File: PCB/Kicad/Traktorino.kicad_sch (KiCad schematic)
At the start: 5 parts, among them J1 analog_pins, J2 mux_pins, J3 595_pins, J4 d13

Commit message: update elements WIP
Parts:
- removed J1: analog_pins, Pin_Headers:Pin_Header_Straight_1x07_Pitch2.54mm, symbol Traktorino-rescue:CONN_01X07
- removed J2: mux_pins, Pin_Headers:Pin_Header_Straight_1x06_Pitch2.54mm, symbol Traktorino-rescue:CONN_01X06
- removed J3: 595_pins, Pin_Headers:Pin_Header_Straight_1x05_Pitch2.54mm, symbol Traktorino-rescue:CONN_01X05
- removed J4: d13, Pin_Headers:Pin_Header_Straight_1x03_Pitch2.54mm, symbol Traktorino-rescue:CONN_01X03
- removed SHIELD1: ARDUINO_SHIELD, arduino_shields:ARDUINO_SHIELD_2_040pins, symbol Traktorino-rescue:ARDUINO_SHIELD
- added A1: Arduino_UNO_R3, Module:Arduino_UNO_R2, symbol MCU_Module:Arduino_UNO_R2
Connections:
- net A0: now also A1.9 (A0)
- net A1: now also A1.10 (A1)
- net A2: now also A1.11 (A2)
- net A3: now also A1.12 (A3)
- net A4: now also A1.13 (SDA/A4)
- net A5: now also A1.14 (SCL/A5)
- net D11: now also A1.26 (D11)
- net D12: now also A1.27 (D12)
- net D13: now also A1.28 (D13)
- net D2: now also A1.17 (D2)
- net D3: now also A1.18 (D3)
- net D4: now also A1.19 (D4)
- net D5: now also A1.20 (D5)
- net D6: now also A1.21 (D6)
- net D7: now also A1.22 (D7)
- net D8: now also A1.23 (D8)
- net GND: now also A1.29 (GND), A1.6 (GND), A1.7 (GND)
- new net +5V: A1.5 (+5V)
- new net D10: A1.25 (D10)
- new net D9: A1.24 (D9)
- no-connect marks 0 -> 7

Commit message: progress
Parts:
- A1: footprint Module:Arduino_UNO_R2 -> Module:Arduino_UNO_R3_WithMountingHoles; symbol MCU_Module:Arduino_UNO_R2 -> MCU_Module:Arduino_UNO_R3
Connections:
- net A5: no longer names the net of A1.14 (SCL/A5)
- net D10: no longer names the net of A1.25 (D10)
- net D13: no longer names the net of A1.28 (D13)
- net D9: no longer names the net of A1.24 (D9)
- no-connect marks 7 -> 13

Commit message: mod layout
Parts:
- removed A1: Arduino_UNO_R3, Module:Arduino_UNO_R3_WithMountingHoles, symbol MCU_Module:Arduino_UNO_R3
- added J1: Power, Connector_PinHeader_2.54mm:PinHeader_1x08_P2.54mm_Vertical, symbol Connector_Generic:Conn_01x08
- added J2: Analog IN, Connector_PinHeader_2.54mm:PinHeader_1x06_P2.54mm_Vertical, symbol Connector_Generic:Conn_01x06
- added J3: Digital 8-end, Connector_PinHeader_2.54mm:PinHeader_1x10_P2.54mm_Vertical, symbol Connector_Generic:Conn_01x10
- added J4: Digital 0-7, Connector_PinHeader_2.54mm:PinHeader_1x08_P2.54mm_Vertical, symbol Connector_Generic:Conn_01x08
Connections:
- net +5V: now also J1.5 (Pin_5)
- net A0: now also J2.1 (Pin_1)
- net A1: now also J2.2 (Pin_2)
- net A2: now also J2.3 (Pin_3)
- net A3: now also J2.4 (Pin_4)
- net A4: now also J2.5 (Pin_5)
- net D11: now also J3.4 (Pin_4)
- net D12: now also J3.5 (Pin_5)
- net D2: now also J4.3 (Pin_3)
- net D3: now also J4.4 (Pin_4)
- net D4: now also J4.5 (Pin_5)
- net D5: now also J4.6 (Pin_6)
- net D6: now also J4.7 (Pin_7)
- net D7: now also J4.8 (Pin_8)
- net D8: now also J3.1 (Pin_1)
- net GND: now also J1.6 (Pin_6), J1.7 (Pin_7), J3.7 (Pin_7)
- no-connect marks 13 -> 14

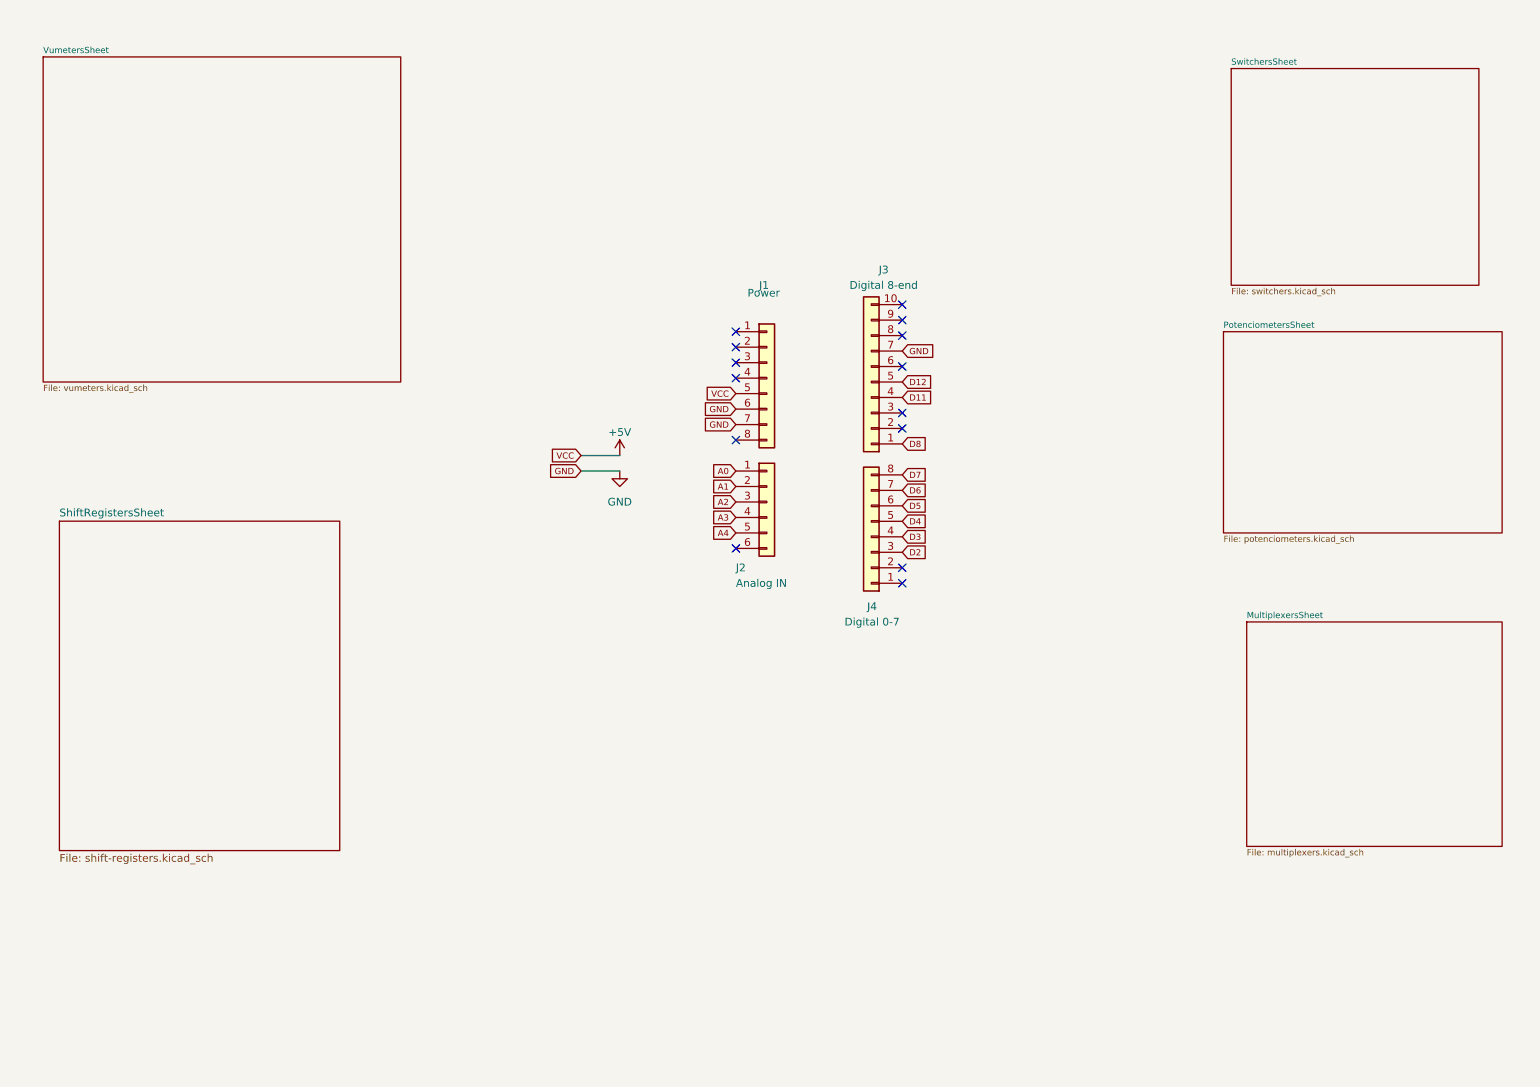
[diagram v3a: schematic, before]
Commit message: Arduino mega retrofit WIP
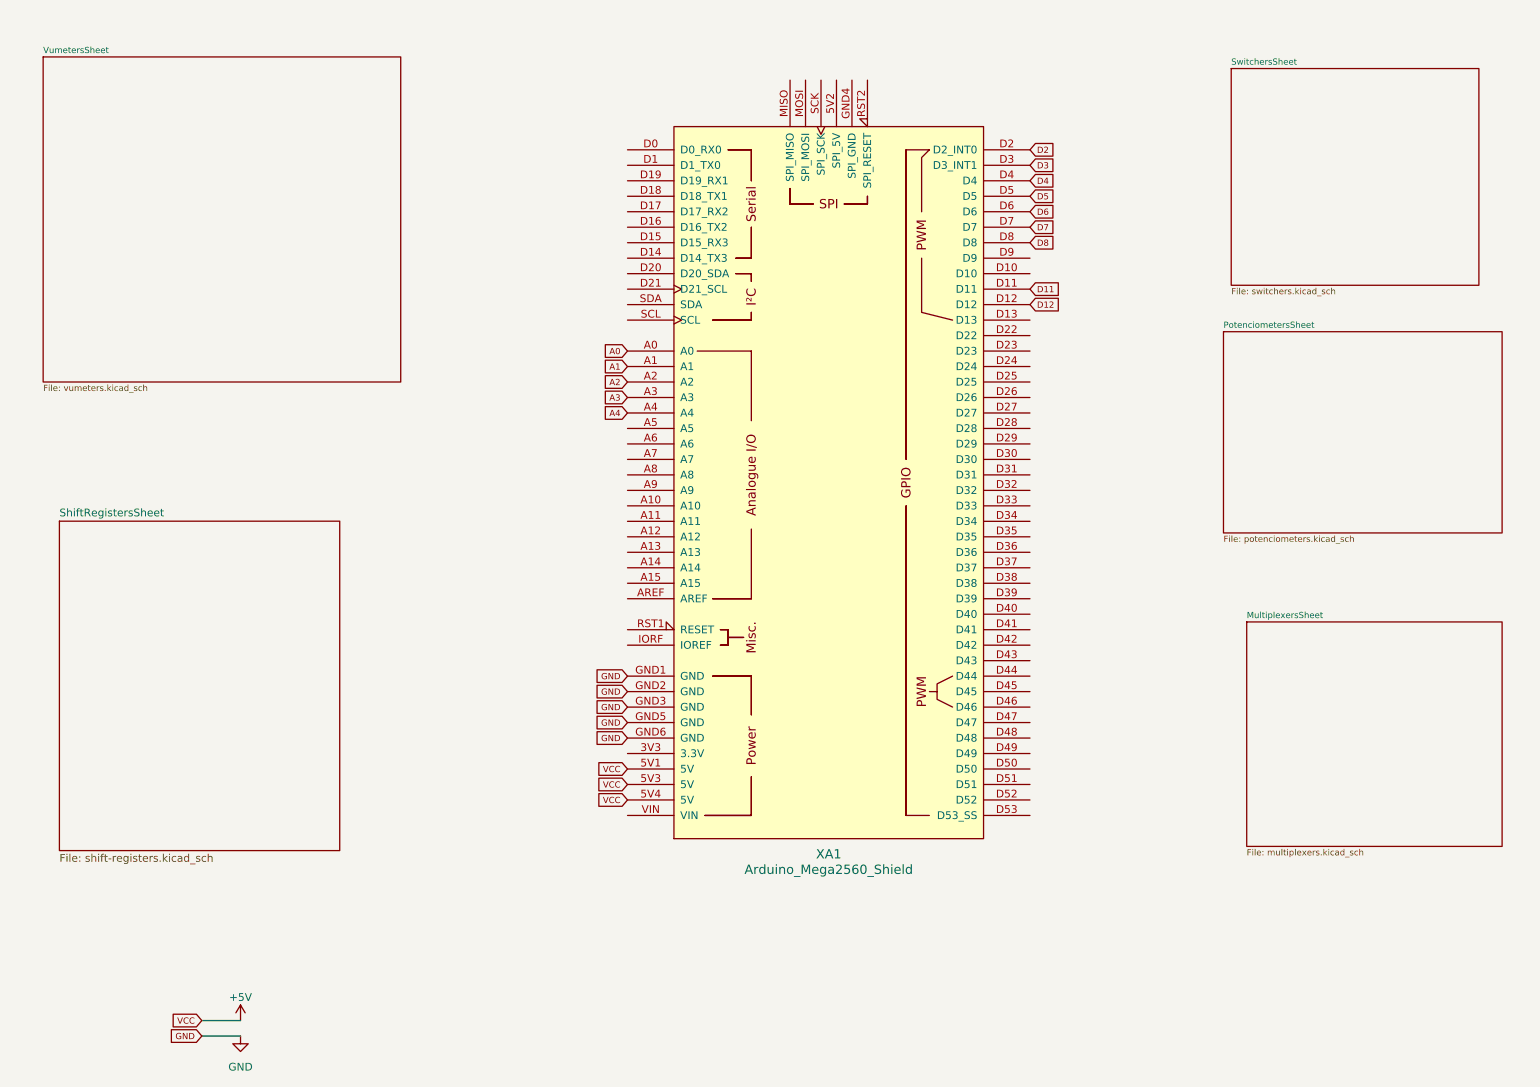
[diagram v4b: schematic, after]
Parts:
- removed J1: Power, Connector_PinHeader_2.54mm:PinHeader_1x08_P2.54mm_Vertical, symbol Connector_Generic:Conn_01x08
- removed J2: Analog IN, Connector_PinHeader_2.54mm:PinHeader_1x06_P2.54mm_Vertical, symbol Connector_Generic:Conn_01x06
- removed J3: Digital 8-end, Connector_PinHeader_2.54mm:PinHeader_1x10_P2.54mm_Vertical, symbol Connector_Generic:Conn_01x10
- removed J4: Digital 0-7, Connector_PinHeader_2.54mm:PinHeader_1x08_P2.54mm_Vertical, symbol Connector_Generic:Conn_01x08
- added XA1: Arduino_Mega2560_Shield, Arduino:Arduino_Mega2560_Shield, symbol arduino:Arduino_Mega2560_Shield
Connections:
- net +5V: now also XA1.5V1 (5V), XA1.5V3 (5V), XA1.5V4 (5V)
- net A0: now also XA1.A0
- net A1: now also XA1.A1
- net A2: now also XA1.A2
- net A3: now also XA1.A3
- net A4: now also XA1.A4
- net D11: now also XA1.D11
- net D12: now also XA1.D12
- net D2: now also XA1.D2 (D2_INT0)
- net D3: now also XA1.D3 (D3_INT1)
- net D4: now also XA1.D4
- net D5: now also XA1.D5
- net D6: now also XA1.D6
- net D7: now also XA1.D7
- net D8: now also XA1.D8
- net GND: now also XA1.GND1 (GND), XA1.GND2 (GND), XA1.GND3 (GND), XA1.GND5 (GND), XA1.GND6 (GND)
- no-connect marks 14 -> 0

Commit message: trillbar added
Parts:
- added IC-POTS-1: 74HC4067D,653, Package_SO:SOIC-24W_7.5x15.4mm_P1.27mm, symbol SamacSys_Parts:74HC4067D,653
- added TB1: trillbar-left, Library:trillbar, symbol traktorino-mk2:trillbar
- added TB2: trillbar-right, Library:trillbar, symbol traktorino-mk2:trillbar
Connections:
- net +5V: now also IC-POTS-1.24 (VCC), TB1.3 (VCC), TB2.3 (VCC)
- net GND: now also IC-POTS-1.12 (GND), IC-POTS-1.15 (~E), TB1.4 (GND), TB2.4 (GND)
- net PFX-1R: now reaches XA1.A10
- net PFX-2R: now reaches XA1.A11
- net PFX-3R: now reaches XA1.A12
- net PMASTER: now reaches XA1.A13
- net A14: now reaches XA1.A14
- net SF-DATA: now reaches XA1.A15
- net TRE-L2: now reaches XA1.A5
- net TRE-L3: now reaches XA1.A6
- net PFX-1L: now reaches XA1.A7
- net PFX-2L: now reaches XA1.A8
- net PFX-3L: now reaches XA1.A9
- net SWFX2-R: now reaches XA1.D0 (D0_RX0)
- net SWFX3-R: now reaches XA1.D1 (D1_TX0)
- net SW_BROWSER_L: now reaches XA1.D10
- net BROWSER_B: now reaches XA1.D13
- net SWFX1-R: now reaches XA1.D14 (D14_TX3)
- net SWPAD-R5: now reaches XA1.D15 (D15_RX3)
- net SWPAD-R4: now reaches XA1.D16 (D16_TX2)
- net SWPAD-R3: now reaches XA1.D17 (D17_RX2)
- net SWPAD-R2: now reaches XA1.D18 (D18_TX1)
- net SWPAD-R1: now reaches XA1.D19 (D19_RX1)
- net SDA: now reaches XA1.D20 (D20_SDA)
- net SDA: now also TB1.2 (SDA), TB2.2 (SDA)
- net SCL: now reaches XA1.D21 (D21_SCL)
- net SCL: now also TB1.1 (SCL), TB2.1 (SCL)
- net SWPAD-R6: now reaches XA1.D22
- net SWPAD-R7: now reaches XA1.D23
- net SWPAD-R8: now reaches XA1.D24
- net SWPAD-L1: now reaches XA1.D25
- net SWPAD-L2: now reaches XA1.D26
- net SWPAD-L3: now reaches XA1.D27
- net SWPAD-L4: now reaches XA1.D28
- net SWPAD-L5: now reaches XA1.D29
- net SWPAD-L6: now reaches XA1.D30
- net SWPAD-L7: now reaches XA1.D31
- net SWPAD-L8: now reaches XA1.D32
- net SWPLAY-L: now reaches XA1.D33
- net SWCUE-L: now reaches XA1.D34
- net SWSHIFT-L: now reaches XA1.D35
- net SWSYNC-L: now reaches XA1.D36
- net SWRANGE-L: now reaches XA1.D37
- net SWPLAY-R: now reaches XA1.D38
- net SWCUE-R: now reaches XA1.D39
- net SWSHIFT-R: now reaches XA1.D40
- net SWSYNC-R: now reaches XA1.D41
- net SWRANGE-R: now reaches XA1.D42
- net SWPRECUE-L1: now reaches XA1.D43
- net SWPRECUE-L2: now reaches XA1.D44
- net SWPRECUE-L3: now reaches XA1.D45
- net SIG_PAD_LED_L: now reaches XA1.D46
- net SIG_PAD_LED_R: now reaches XA1.D47
- net MPLEX-S0: now reaches XA1.D48
- net MPLEX-S0: now also IC-POTS-1.10 (S0)
- net MPLEX-S1: now reaches XA1.D49
- net MPLEX-S1: now also IC-POTS-1.11 (S1)
- net MPLEX-S2: now reaches XA1.D50
- net MPLEX-S2: now also IC-POTS-1.14 (S2)
- net MPLEX-S3: now reaches XA1.D51
- net MPLEX-S3: now also IC-POTS-1.13 (S3)
- net SF-CLOCK: now reaches XA1.D52
- net SF-LATCH: now reaches XA1.D53 (D53_SS)
- net SWBR-PREVIEW: now reaches XA1.D9
- net A0 renamed MPLEX-A0
- net MPLEX-A0: now also IC-POTS-1.1 (Z)
- net A1 renamed GAIN-L1
- net A2 renamed GAIN-L2
- net A3 renamed GAIN-L3
- net A4 renamed TRE-L1
- net D11 renamed SW_BROWSER_R
- net D12 renamed BROWSER_A
- net D2 renamed SWSEL-L3
- net D3 renamed SWSEL-L2
- net D4 renamed SWSEL-L1
- net D5 renamed SWFX3-L
- net D6 renamed SWFX2-L
- net D7 renamed SWFX1-L
- net D8 renamed SWBR-BACK
- new net BAS-L1: IC-POTS-1.21 (Y10)
- new net BAS-L2: IC-POTS-1.20 (Y11)
- new net BAS-L3: IC-POTS-1.19 (Y12)
- new net FADER-L1: IC-POTS-1.8 (Y1)
- new net FADER-L2: IC-POTS-1.7 (Y2)
- new net FADER-L3: IC-POTS-1.6 (Y3)
- new net FILTER-L1: IC-POTS-1.2 (Y7)
- new net FILTER-L2: IC-POTS-1.23 (Y8)
- new net FILTER-L3: IC-POTS-1.22 (Y9)
- new net MID-L1: IC-POTS-1.18 (Y13)
- new net MID-L2: IC-POTS-1.17 (Y14)
- new net MID-L3: IC-POTS-1.16 (Y15)
- new net PITCH-L: IC-POTS-1.9 (Y0)
- new net PITCH-R: IC-POTS-1.3 (Y6)
- new net PMIX-HP: IC-POTS-1.5 (Y4)
- new net PVOL-HP: IC-POTS-1.4 (Y5)
- no-connect marks 0 -> 7
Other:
- sheet VumetersSheet renamed LedsSheet
- removed sheet MultiplexersSheet
- added sheet PadLedsSheet (pad-leds.kicad_sch)
- sheet LedsSheet: file vumeters.kicad_sch -> leds.kicad_sch

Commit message: board updated
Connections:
- net FADER-L1: now also IC-POTS-1.4 (Y5); no longer IC-POTS-1.8 (Y1)
- net FADER-L2: now also IC-POTS-1.5 (Y4); no longer IC-POTS-1.7 (Y2)
- net MPLEX-S0: now also XA1.D47; no longer XA1.D48
- net MPLEX-S2: now also XA1.D51; no longer XA1.D50
- net MPLEX-S3: now also XA1.D53 (D53_SS); no longer XA1.D51
- net PITCH-L: now also IC-POTS-1.3 (Y6); no longer IC-POTS-1.9 (Y0)
- net PITCH-R: now also IC-POTS-1.9 (Y0); no longer IC-POTS-1.3 (Y6)
- net PMASTER: now also XA1.A15; no longer XA1.A13
- net PMIX-HP: now also IC-POTS-1.8 (Y1); no longer IC-POTS-1.5 (Y4)
- net PVOL-HP: now also IC-POTS-1.7 (Y2); no longer IC-POTS-1.4 (Y5)
- net SF-DATA: now also XA1.A13; no longer XA1.A15
- net SF-LATCH: now also XA1.D50; no longer XA1.D53 (D53_SS)
- net SIG_PAD_LED_L: now also XA1.D48; no longer XA1.D46
- net SIG_PAD_LED_R: now also XA1.D46; no longer XA1.D47
- net SWPAD-L1: now also XA1.D24; no longer XA1.D25
- net SWPAD-L2: now also XA1.D25; no longer XA1.D26
- net SWPAD-L3: now also XA1.D26; no longer XA1.D27
- net SWPAD-L4: now also XA1.D27; no longer XA1.D28
- net SWPAD-L6: now also XA1.D28; no longer XA1.D30
- net SWPAD-L7: now also XA1.D30; no longer XA1.D31
- net SWPAD-L8: now also XA1.D31; no longer XA1.D32
- net SWPAD-R8: now also XA1.D32; no longer XA1.D24
- net A14: no longer names the net of XA1.A14
- no-connect marks 7 -> 8
